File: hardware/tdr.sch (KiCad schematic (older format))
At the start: 0 parts

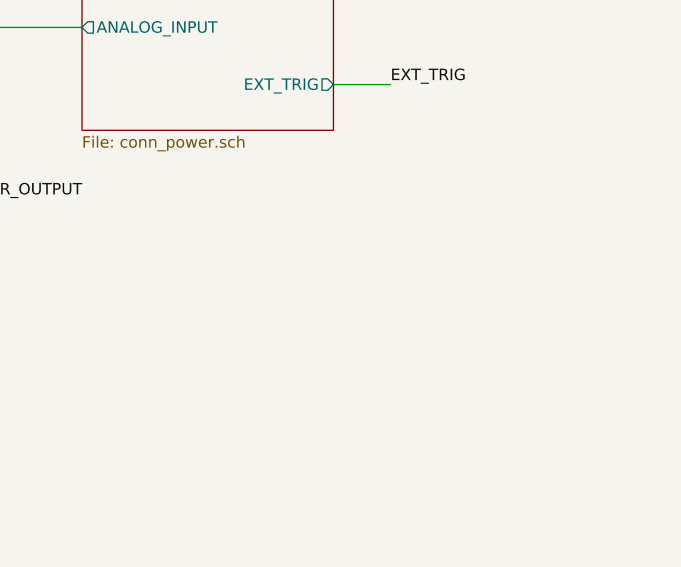
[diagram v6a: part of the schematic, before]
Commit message: added picture of assembled pcb, started erratum for r0..
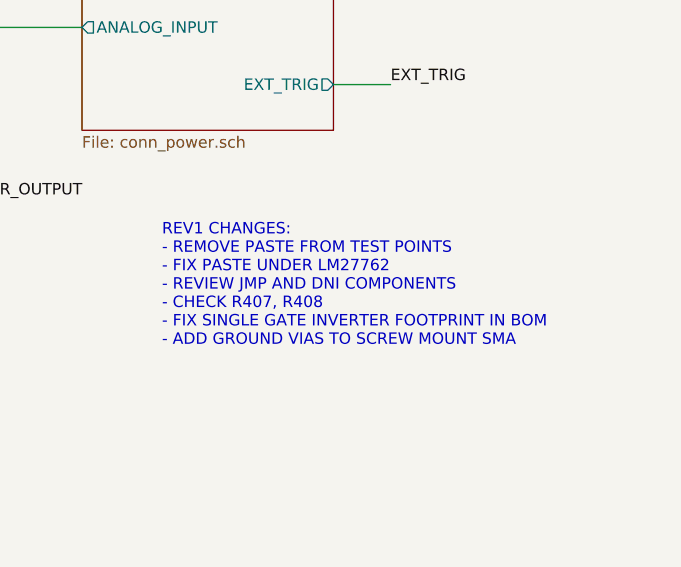
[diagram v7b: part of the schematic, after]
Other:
- note added: "REV1 CHANGES:\n- REMOVE PASTE FROM TEST POINTS\n- FIX PASTE UNDER LM27762\n- REVIEW JMP AND DNI COMPONENTS\n- CHECK R407, R408\n- FIX SINGLE GATE INVERTER FOOTPRINT IN BOM\n- ADD GROUND VIAS TO SCREW MOUNT SMA"
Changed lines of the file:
@@
 Text Label 6050 3050 0    50   ~ 0
 LATCH
+Text Notes 8750 6300 0    50   ~ 0
+REV1 CHANGES:\n- REMOVE PASTE FROM TEST POINTS\n- FIX PASTE UNDER LM27762\n- REVIEW JMP AND DNI COMPONENTS\n- CHECK R407, R408\n- FIX SINGLE GATE INVERTER FOOTPRINT IN BOM\n- ADD GROUND VIAS TO SCREW MOUNT SMA
 $EndSCHEMATC
